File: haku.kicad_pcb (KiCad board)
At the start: 2 copper layers, 172 parts, among them SW1 SW_Push, U1 ATmega32U4-AU, U2 SRV05-4, Y1 16MHz

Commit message: begin routing
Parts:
- moved SW1 83.4 mm to (141.1, 161.9)
- moved R6 75.8 mm to (142.2, 166.0), turned to 180 degrees
- moved D26 19.1 mm to (111.1, 154.0)
- moved D21 19.0 mm to (108.0, 154.0)
- moved D24 17.5 mm to (133.3, 115.9)
- moved R10 7.91 mm to (113.5, 91.2), turned to 270 degrees
- moved R4 7.25 mm to (115.5, 119.6)
- moved R5 7.25 mm to (113.1, 119.6)
- moved R9 6.38 mm to (94.5, 91.2), turned to 270 degrees
- moved C2 4.55 mm to (157.1, 180.2), turned to 315 degrees
- moved C4 4.53 mm to (144.8, 177.3)
- moved C8 4.53 mm to (146.4, 178.8)
- moved U2 2.07 mm to (105.2, 102.7)
- moved F1 1.91 mm to (102.9, 98.2)
- moved R8 1.81 mm to (168.9, 166.3)
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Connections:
- net Net-(R4-Pad1) renamed /D1+
- net Net-(R5-Pad1) renamed /D1-
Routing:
- net Col0: track 0.00 -> 206.6 mm
- net +5V: track 0.00 -> 196.6 mm, vias 0 -> 9
- net GND: track 0.00 -> 105.7 mm
- net Col1: track 0.00 -> 86.1 mm
- net /D1-: track 0.00 -> 83.4 mm
- net /D1+: track 0.00 -> 82.4 mm
- net D+: track 4.12 -> 36.7 mm
- net D-: track 4.02 -> 34.3 mm
- net Net-(R6-Pad2): track 0.00 -> 20.3 mm
- net Net-(R9-Pad2): track 0.00 -> 12.9 mm, vias 0 -> 2
- net Net-(U1-Pad8): track 0.00 -> 11.8 mm
- net Net-(U1-Pad9): track 0.00 -> 10.7 mm
- net Net-(U1-Pad10): track 0.00 -> 9.61 mm
- net Net-(R10-Pad2): track 0.00 -> 9.44 mm
- net Net-(C8-Pad1): track 0.00 -> 8.71 mm, vias 0 -> 2
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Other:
- board outline added: 323.9 x 97 mm

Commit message: complete routing
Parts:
- R2, R3, R7: moved to B.Cu
- moved R1 176.1 mm to (156.3, 139.4)
- moved D26 19.6 mm to (130.7, 154.1)
- moved D19 19.6 mm to (112.9, 112.4)
- moved D21 19.0 mm to (127.0, 154.0)
- moved D24 17.9 mm to (115.8, 112.4)
- moved D68 15.9 mm to (350.8, 173.0)
- moved D71 12.5 mm to (353.9, 96.8), turned to 90 degrees
- moved R7 7.59 mm to (344.3, 94.7), turned to 90 degrees
- moved R3 7.34 mm to (344.3, 103.0)
- moved C4 3.07 mm to (142.9, 174.9)
- moved C8 2.92 mm to (144.4, 176.7)
- moved R4 2.60 mm to (115.5, 122.2)
- moved R5 2.60 mm to (113.1, 122.2)
- moved R2 2.12 mm to (351.3, 107.4), turned to 90 degrees
- moved D72 1.59 mm to (352.4, 115.9)
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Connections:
- U1 pad 1: Net-(U1-Pad1) -> IND_LED3
- U1 pad 10: Net-(U1-Pad10) -> Row6
- U1 pad 11: Net-(U1-Pad11) -> Col1
- U1 pad 18: Net-(U1-Pad18) -> LED_DIN
- U1 pad 19: Net-(U1-Pad19) -> Row0
- U1 pad 20: Net-(U1-Pad20) -> Row1
- U1 pad 25: Net-(U1-Pad25) -> Row2
- U1 pad 26: Net-(U1-Pad26) -> Row3
- U1 pad 27: Net-(U1-Pad27) -> IND_LED1
- U1 pad 28: Net-(U1-Pad28) -> IND_LED2
- U1 pad 29: Net-(U1-Pad29) -> Row5
- U1 pad 30: Net-(U1-Pad30) -> Row4
- U1 pad 31: Net-(U1-Pad31) -> Col4
- U1 pad 32: Net-(U1-Pad32) -> Col7
- U1 pad 36: Net-(U1-Pad36) -> Col2
- U1 pad 37: Net-(U1-Pad37) -> Col6
- U1 pad 38: Net-(U1-Pad38) -> Col5
- U1 pad 39: Net-(U1-Pad39) -> Col3
- U1 pad 40: Net-(U1-Pad40) -> Row8
- U1 pad 41: Net-(U1-Pad41) -> Row9
- U1 pad 8: Net-(U1-Pad8) -> Col0
- U1 pad 9: Net-(U1-Pad9) -> Row7
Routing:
- net Row4: track 0.00 -> 473.6 mm, vias 0 -> 4
- net Row5: track 0.00 -> 379.1 mm, vias 0 -> 6
- net Col6: track 0.00 -> 367.9 mm
- net Col7: track 0.00 -> 366.8 mm
- net Row1: track 0.00 -> 361.6 mm, vias 0 -> 4
- net Row0: track 0.00 -> 360.7 mm, vias 0 -> 4
- net Row2: track 0.00 -> 353.4 mm, vias 0 -> 4
- net Row7: track 0.00 -> 351.2 mm, vias 0 -> 4
- net IND_LED3: track 0.00 -> 335.2 mm, vias 0 -> 2
- net +5V: track 196.6 -> 512.2 mm, vias 9 -> 15
- net Row8: track 0.00 -> 311.5 mm, vias 0 -> 2
- net Row6: track 0.00 -> 302.9 mm, vias 0 -> 2
- net Row3: track 0.00 -> 292.1 mm, vias 0 -> 4
- net IND_LED2: track 0.00 -> 290.6 mm
- net Row9: track 0.00 -> 281.7 mm, vias 0 -> 2
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
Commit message: ground fills
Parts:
- moved R3 7.06 mm to (351.3, 102.0), turned to 90 degrees
- moved R6 2.54 mm to (139.6, 166.0)
- moved D5 2.34 mm to (347.7, 109.5)
- moved R2 2.16 mm to (351.3, 109.6)
- moved SW1 1.79 mm to (139.9, 160.7)
- moved D6 1.19 mm to (347.7, 102.0)
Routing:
- net Net-(D24-Pad2): track 0.09 -> 10.7 mm
- net GND: track 140.5 -> 149.6 mm, vias 0 -> 12
- net IND_LED2: track 290.6 -> 284.7 mm
- net Net-(D19-Pad2): track 0.00 -> 5.61 mm, vias 0 -> 1
- net Col6: track 367.9 -> 363.0 mm
- net IND_LED1: track 279.1 -> 275.1 mm
- net Row1: track 361.6 -> 357.8 mm
- net Row2: track 353.4 -> 349.7 mm
- net Col0: track 282.5 -> 278.9 mm
- net Col1: track 206.3 -> 202.8 mm
- net Col5: track 262.6 -> 259.3 mm
- net Col3: track 204.1 -> 200.8 mm
- net Col2: track 188.3 -> 185.3 mm
- net Row0: track 360.7 -> 357.9 mm
- net Col4: track 230.6 -> 227.9 mm
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- added copper zone on B.Cu, net GND
- added copper zone on F.Cu, net GND

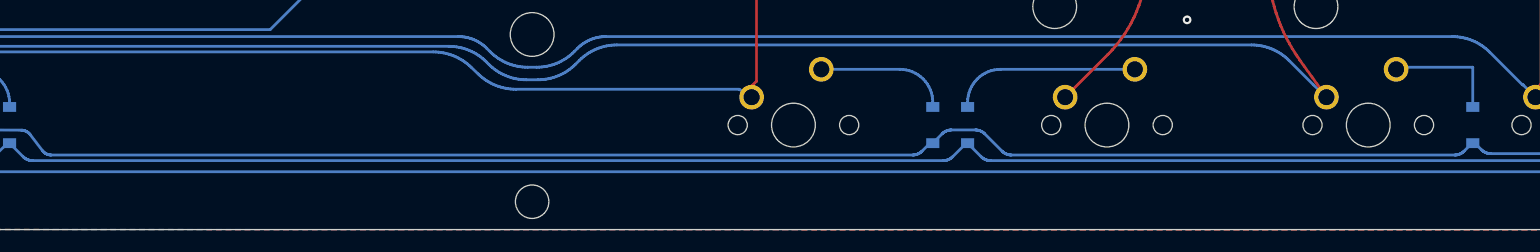
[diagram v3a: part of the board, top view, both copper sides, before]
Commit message: messing with silkscreen (will likely change)
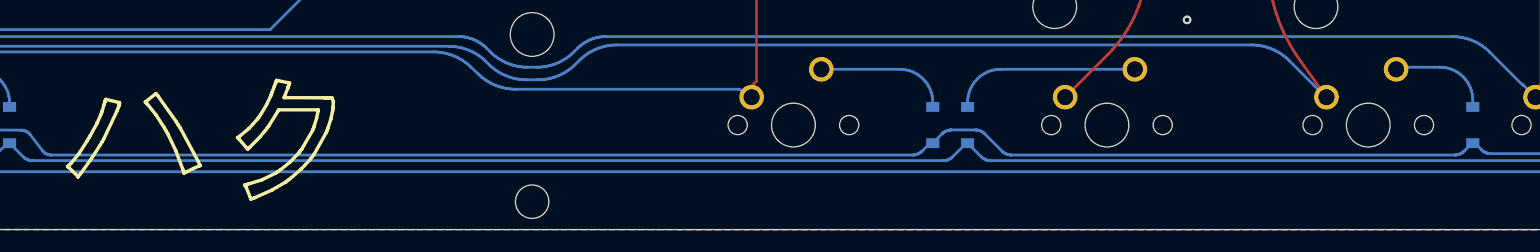
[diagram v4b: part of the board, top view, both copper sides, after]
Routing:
- net Net-(D66-Pad2): track 10.7 -> 9.39 mm

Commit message: update data lines
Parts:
- moved R7 5.21 mm to (349.5, 94.7)
- moved D5 1.40 mm to (346.3, 109.5)
- moved D6 1.40 mm to (346.3, 102.0)
- moved D7 1.40 mm to (346.3, 94.5)
- moved R2 1.40 mm to (349.9, 109.6)
- moved R3 1.40 mm to (349.9, 102.0)
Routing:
- net IND_LED3: track 332.9 -> 328.5 mm
- net +5V: track 511.9 -> 510.3 mm
- net IND_LED2: track 284.7 -> 286.1 mm
- net IND_LED1: track 275.1 -> 276.4 mm
- net /D1-: track 80.8 -> 80.2 mm
- net /D1+: track 79.8 -> 79.2 mm
- net GND: vias 12 -> 15

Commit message: nudges some traces
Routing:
- net IND_LED3: track 328.5 -> 327.2 mm
- net Col2: track 185.3 -> 186.1 mm
- net GND: vias 15 -> 16
